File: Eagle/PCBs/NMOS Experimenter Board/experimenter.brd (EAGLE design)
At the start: 49.5 x 66 mm, 384 parts, among them Q10 2N7002, Q11 2N7002, Q12 2N7002, Q13 2N7002, Q14 2N7002, Q15 2N7002, Q16 2N7002, Q17 2N7002, Q18 2N7002, Q19 2N7002, Q2 2N7002, Q20 2N7002, Q21 2N7002, Q22 2N7002, Q23 2N7002, Q24 2N7002, Q25 2N7002, Q3 2N7002, Q4 2N7002, Q5 2N7002, Q6 2N7002, Q7 2N7002, Q8 2N7002, Q9 2N7002

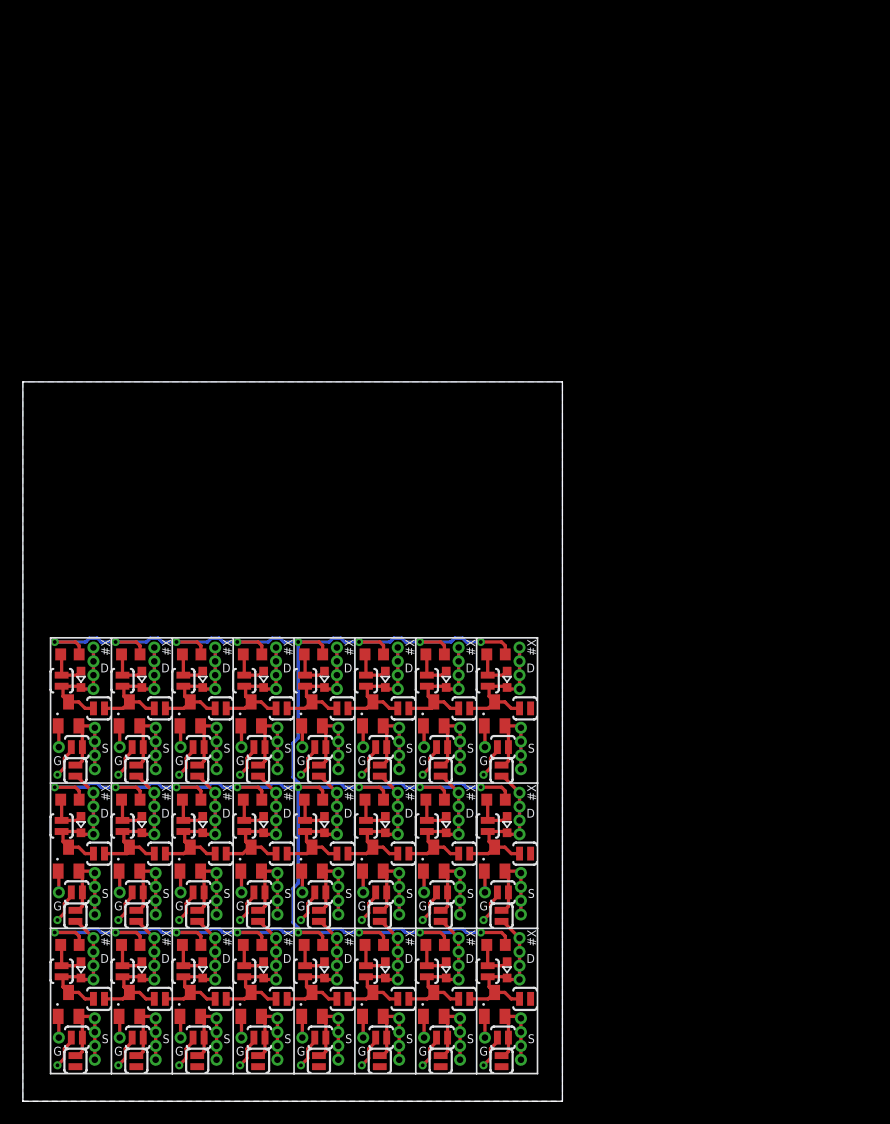
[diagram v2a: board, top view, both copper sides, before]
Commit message: A 6x12 grid fits
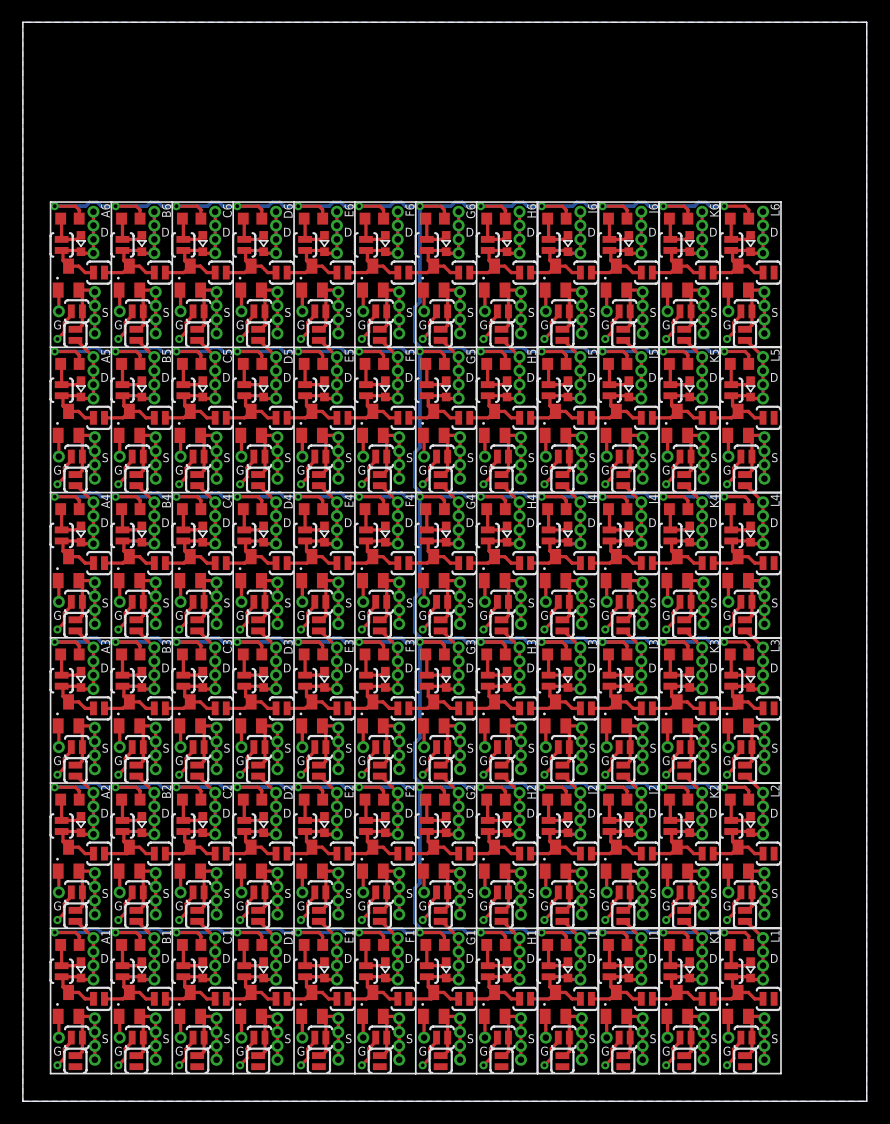
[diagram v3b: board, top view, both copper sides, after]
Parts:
- added D26, D27, D28, D29, D30, D31, D32, D33, D34, D35, D36, D37, D38, D39, D40, D41, D42, D43, D44, D45, D46, D47, D48, D49, D50, D51, D52, D53, D54, D55, D56, D57, D58, D59, D60, D61, D62, D63, D64, D65, D66, D67, D68, D69, D70, D71, D72, D73: (no value), ellajameson-core:CHIP-LED0603
- added DRAINA26, DRAINA27, DRAINA28, DRAINA29, DRAINA30, DRAINA31, DRAINA32, DRAINA33, DRAINA34, DRAINA35, DRAINA36, DRAINA37, DRAINA38, DRAINA39, DRAINA40, DRAINA41, DRAINA42, DRAINA43, DRAINA44, DRAINA45, DRAINA46, DRAINA47, DRAINA48, DRAINA49, DRAINA50, DRAINA51, DRAINA52, DRAINA53, DRAINA54, DRAINA55, DRAINA56, DRAINA57, DRAINA58, DRAINA59, DRAINA60, DRAINA61, DRAINA62, DRAINA63, DRAINA64, DRAINA65, DRAINA66, DRAINA67, DRAINA68, DRAINA69, DRAINA70, DRAINA71, DRAINA72, DRAINA73, DRAINB26, DRAINB27, DRAINB28, DRAINB29, DRAINB30, DRAINB31, DRAINB32, DRAINB33, DRAINB34, DRAINB35, DRAINB36, DRAINB37, DRAINB38, DRAINB39, DRAINB40, DRAINB41, DRAINB42, DRAINB43, DRAINB44, DRAINB45, DRAINB46, DRAINB47, DRAINB48, DRAINB49, DRAINB50, DRAINB51, DRAINB52, DRAINB53, DRAINB54, DRAINB55, DRAINB56, DRAINB57, DRAINB58, DRAINB59, DRAINB60, DRAINB61, DRAINB62, DRAINB63, DRAINB64, DRAINB65, DRAINB66, DRAINB67, DRAINB68, DRAINB69, DRAINB70, DRAINB71, DRAINB72, DRAINB73, DRAINC26, DRAINC27, DRAINC28, DRAINC29, DRAINC30, DRAINC31, DRAINC32, DRAINC33, DRAINC34, DRAINC35, DRAINC36, DRAINC37, DRAINC38, DRAINC39, DRAINC40, DRAINC41, DRAINC42, DRAINC43, DRAINC44, DRAINC45, DRAINC46, DRAINC47, DRAINC48, DRAINC49, DRAINC50, DRAINC51, DRAINC52, DRAINC53, DRAINC54, DRAINC55, DRAINC56, DRAINC57, DRAINC58, DRAINC59, DRAINC60, DRAINC61, DRAINC62, DRAINC63, DRAINC64, DRAINC65, DRAINC66, DRAINC67, DRAINC68, DRAINC69, DRAINC70, DRAINC71, DRAINC72, DRAINC73, DRAIND26, DRAIND27, DRAIND28, DRAIND29, DRAIND30, DRAIND31, DRAIND32, DRAIND33, DRAIND34, DRAIND35, DRAIND36, DRAIND37, DRAIND38, DRAIND39, DRAIND40, DRAIND41, DRAIND42, DRAIND43, DRAIND44, DRAIND45, DRAIND46, DRAIND47, DRAIND48, DRAIND49, DRAIND50, DRAIND51, DRAIND52, DRAIND53, DRAIND54, DRAIND55, DRAIND56, DRAIND57, DRAIND58, DRAIND59, DRAIND60, DRAIND61, DRAIND62, DRAIND63, DRAIND64, DRAIND65, DRAIND66, DRAIND67, DRAIND68, DRAIND69, DRAIND70, DRAIND71, DRAIND72, DRAIND73, GATE26, GATE27, GATE28, GATE29, GATE30, GATE31, GATE32, GATE33, GATE34, GATE35, GATE36, GATE37, GATE38, GATE39, GATE40, GATE41, GATE42, GATE43, GATE44, GATE45, GATE46, GATE47, GATE48, GATE49, GATE50, GATE51, GATE52, GATE53, GATE54, GATE55, GATE56, GATE57, GATE58, GATE59, GATE60, GATE61, GATE62, GATE63, GATE64, GATE65, GATE66, GATE67, GATE68, GATE69, GATE70, GATE71, GATE72, GATE73, SOURCEA26, SOURCEA27, SOURCEA28, SOURCEA29, SOURCEA30, SOURCEA31, SOURCEA32, SOURCEA33, SOURCEA34, SOURCEA35, SOURCEA36, SOURCEA37, SOURCEA38, SOURCEA39, SOURCEA40, SOURCEA41, SOURCEA42, SOURCEA43, SOURCEA44, SOURCEA45, SOURCEA46, SOURCEA47, SOURCEA48, SOURCEA49, SOURCEA50, SOURCEA51, SOURCEA52, SOURCEA53, SOURCEA54, SOURCEA55, SOURCEA56, SOURCEA57, SOURCEA58, SOURCEA59, SOURCEA60, SOURCEA61, SOURCEA62, SOURCEA63, SOURCEA64, SOURCEA65, SOURCEA66, SOURCEA67, SOURCEA68, SOURCEA69, SOURCEA70, SOURCEA71, SOURCEA72, SOURCEA73, SOURCEB26, SOURCEB27, SOURCEB28, SOURCEB29, SOURCEB30, SOURCEB31, SOURCEB32, SOURCEB33, SOURCEB34, SOURCEB35, SOURCEB36, SOURCEB37, SOURCEB38, SOURCEB39, SOURCEB40, SOURCEB41, SOURCEB42, SOURCEB43, SOURCEB44, SOURCEB45, SOURCEB46, SOURCEB47, SOURCEB48, SOURCEB49, SOURCEB50, SOURCEB51, SOURCEB52, SOURCEB53, SOURCEB54, SOURCEB55, SOURCEB56, SOURCEB57, SOURCEB58, SOURCEB59, SOURCEB60, SOURCEB61, SOURCEB62, SOURCEB63, SOURCEB64, SOURCEB65, SOURCEB66, SOURCEB67, SOURCEB68, SOURCEB69, SOURCEB70, SOURCEB71, SOURCEB72, SOURCEB73, SOURCEC26, SOURCEC27, SOURCEC28, SOURCEC29, SOURCEC30, SOURCEC31, SOURCEC32, SOURCEC33, SOURCEC34, SOURCEC35, SOURCEC36, SOURCEC37, SOURCEC38, SOURCEC39, SOURCEC40, SOURCEC41, SOURCEC42, SOURCEC43, SOURCEC44, SOURCEC45, SOURCEC46, SOURCEC47, SOURCEC48, SOURCEC49, SOURCEC50, SOURCEC51, SOURCEC52, SOURCEC53, SOURCEC54, SOURCEC55, SOURCEC56, SOURCEC57, SOURCEC58, SOURCEC59, SOURCEC60, SOURCEC61, SOURCEC62, SOURCEC63, SOURCEC64, SOURCEC65, SOURCEC66, SOURCEC67, SOURCEC68, SOURCEC69, SOURCEC70, SOURCEC71, SOURCEC72, SOURCEC73, SOURCED26, SOURCED27, SOURCED28, SOURCED29, SOURCED30, SOURCED31, SOURCED32, SOURCED33, SOURCED34, SOURCED35, SOURCED36, SOURCED37, SOURCED38, SOURCED39, SOURCED40, SOURCED41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: TPWIRE, ellajameson-core:TP_TH_WIRE
- added JD26, JD27, JD28, JD29, JD30, JD31, JD32, JD33, JD34, JD35, JD36, JD37, JD38, JD39, JD40, JD41, JD42, JD43, JD44, JD45, JD46, JD47, JD48, JD49, JD50, JD51, JD52, JD53, JD54, JD55, JD56, JD57, JD58, JD59, JD60, JD61, JD62, JD63, JD64, JD65, JD66, JD67, JD68, JD69, JD70, JD71, JD72, JD73, JN26, JN27, JN28, JN29, JN30, JN31, JN32, JN33, JN34, JN35, JN36, JN37, JN38, JN39, JN40, JN41, JN42, JN43, JN44, JN45, JN46, JN47, JN48, JN49, JN50, JN51, JN52, JN53, JN54, JN55, JN56, JN57, JN58, JN59, JN60, JN61, JN62, JN63, JN64, JN65, JN66, JN67, JN68, JN69, JN70, JN71, JN72, JN73, JP26, JP27, JP28, JP29, JP30, JP31, JP32, JP33, JP34, JP35, JP36, JP37, JP38, JP39, JP40, JP41, JP42, JP43, JP44, JP45, JP46, JP47, JP48, JP49, JP50, JP51, JP52, JP53, JP54, JP55, JP56, JP57, JP58, JP59, JP60, JP61, JP62, JP63, JP64, JP65, JP66, JP67, JP68, JP69, JP70, JP71, JP72, JP73, JS26, JS27, JS28, JS29, JS30, JS31, JS32, JS33, JS34, JS35, JS36, JS37, JS38, JS39, JS40, JS41, JS42, JS43, JS44, JS45, JS46, JS47, JS48, JS49, JS50, JS51, JS52, JS53, JS54, JS55, JS56, JS57, JS58, JS59, JS60, JS61, JS62, JS63, JS64, JS65, JS66, JS67, JS68, JS69, JS70, JS71, JS72, JS73: SJ_NO, ellajameson-core:SJ_2S-NO
- added Q26, Q27, Q28, Q29, Q30, Q31, Q32, Q33, Q34, Q35, Q36, Q37, Q38, Q39, Q40, Q41, Q42, Q43, Q44, Q45, Q46, Q47, Q48, Q49, Q50, Q51, Q52, Q53, Q54, Q55, Q56, Q57, Q58, Q59, Q60, Q61, Q62, Q63, Q64, Q65, Q66, Q67, Q68, Q69, Q70, Q71, Q72, Q73: 2N7002, ellajameson-core:SOT23
- added R26, R27, R28, R29, R30, R31, R32, R33, R34, R35, R36, R37, R38, R39, R40, R41, R42, R43, R44, R45, R46, R47, R48, R49, R50, R51, R52, R53, R54, R55, R56, R57, R58, R59, R60, R61, R62, R63, R64, R65, R66, R67, R68, R69, R70, R71, R72, R73: (no value), ellajameson-core:R0603
- moved DRAINA12 63.0 mm to (51.2, 81.7)
- moved DRAINA13 63.0 mm to (56.8, 81.7)
- moved DRAINB12 63.0 mm to (51.2, 80.4)
- moved DRAINB13 63.0 mm to (56.8, 80.4)
- moved DRAIND12 63.0 mm to (51.2, 77.9)
- moved DRAIND13 63.0 mm to (56.8, 77.9)
- moved JP12 63.0 mm to (48.3, 78.6)
- moved JP13 63.0 mm to (53.8, 78.6)
- moved JS12 63.0 mm to (49.5, 70.4)
- moved JS13 63.0 mm to (55.1, 70.4)
- moved SOURCEA12 63.0 mm to (51.3, 74.3)
- moved SOURCEA13 63.0 mm to (56.9, 74.3)
- moved SOURCEB12 63.0 mm to (51.3, 73.0)
- moved SOURCEB13 63.0 mm to (56.9, 73.0)
- moved SOURCED12 63.0 mm to (51.3, 70.5)
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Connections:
- new net N$101: D26.A, JP26.2, R26.1
- new net N$102: D26.C, DRAINA26.TP, DRAINB26.TP, DRAINC26.TP, DRAIND26.TP, JD26.2, JP26.1, JS34.1, Q26.3
- new net N$103: JN26.2, JS26.2, Q26.2, SOURCEA26.TP, SOURCEB26.TP, SOURCEC26.TP, SOURCED26.TP
- new net N$104: GATE26.TP, Q26.1
- new net N$105: D27.A, JP27.2, R27.1
- new net N$106: D27.C, DRAINA27.TP, DRAINB27.TP, DRAINC27.TP, DRAIND27.TP, JD26.1, JD27.2, JP27.1, JS35.1, Q27.3
- new net N$107: JN27.2, JS27.2, Q27.2, SOURCEA27.TP, SOURCEB27.TP, SOURCEC27.TP, SOURCED27.TP
- new net N$108: GATE27.TP, Q27.1
- new net N$109: D28.A, JP28.2, R28.1
- new net N$110: D28.C, DRAINA28.TP, DRAINB28.TP, DRAINC28.TP, DRAIND28.TP, JD27.1, JD28.2, JP28.1, JS36.1, Q28.3
- new net N$111: JN28.2, JS28.2, Q28.2, SOURCEA28.TP, SOURCEB28.TP, SOURCEC28.TP, SOURCED28.TP
- new net N$112: GATE28.TP, Q28.1
- new net N$113: D29.A, JP29.2, R29.1
- new net N$114: D29.C, DRAINA29.TP, DRAINB29.TP, DRAINC29.TP, DRAIND29.TP, JD28.1, JD29.2, JP29.1, JS37.1, Q29.3
- new net N$115: JN29.2, JS29.2, Q29.2, SOURCEA29.TP, SOURCEB29.TP, SOURCEC29.TP, SOURCED29.TP
- new net N$116: GATE29.TP, Q29.1
- new net N$117: D30.A, JP30.2, R30.1
- new net N$118: D30.C, DRAINA30.TP, DRAINB30.TP, DRAINC30.TP, DRAIND30.TP, JD29.1, JD30.2, JP30.1, JS38.1, Q30.3
- new net N$119: JN30.2, JS30.2, Q30.2, SOURCEA30.TP, SOURCEB30.TP, SOURCEC30.TP, SOURCED30.TP
- new net N$120: GATE30.TP, Q30.1
- new net N$121: D31.A, JP31.2, R31.1
- new net N$122: D31.C, DRAINA31.TP, DRAINB31.TP, DRAINC31.TP, DRAIND31.TP, JD30.1, JD31.2, JP31.1, JS39.1, Q31.3
- new net N$123: JN31.2, JS31.2, Q31.2, SOURCEA31.TP, SOURCEB31.TP, SOURCEC31.TP, SOURCED31.TP
- new net N$124: GATE31.TP, Q31.1
- new net N$125: D32.A, JP32.2, R32.1
- new net N$126: D32.C, DRAINA32.TP, DRAINB32.TP, DRAINC32.TP, DRAIND32.TP, JD31.1, JD32.2, JP32.1, JS40.1, Q32.3
- new net N$127: JN32.2, JS32.2, Q32.2, SOURCEA32.TP, SOURCEB32.TP, SOURCEC32.TP, SOURCED32.TP
- new net N$128: GATE32.TP, Q32.1
- new net N$129: D33.A, JP33.2, R33.1
- new net N$130: D33.C, DRAINA33.TP, DRAINB33.TP, DRAINC33.TP, DRAIND33.TP, JD32.1, JD33.2, JP33.1, JS41.1, Q33.3
- new net N$131: JN33.2, JS33.2, Q33.2, SOURCEA33.TP, SOURCEB33.TP, SOURCEC33.TP, SOURCED33.TP
- new net N$132: GATE33.TP, Q33.1
- new net N$133: D34.A, JP34.2, R34.1
- new net N$134: D34.C, DRAINA34.TP, DRAINB34.TP, DRAINC34.TP, DRAIND34.TP, JD34.2, JP34.1, JS42.1, Q34.3
- new net N$135: JN34.2, JS34.2, Q34.2, SOURCEA34.TP, SOURCEB34.TP, SOURCEC34.TP, SOURCED34.TP
- new net N$136: GATE34.TP, Q34.1
- new net N$137: D35.A, JP35.2, R35.1
- new net N$138: D35.C, DRAINA35.TP, DRAINB35.TP, DRAINC35.TP, DRAIND35.TP, JD34.1, JD35.2, JP35.1, JS43.1, Q35.3
- new net N$139: JN35.2, JS35.2, Q35.2, SOURCEA35.TP, SOURCEB35.TP, SOURCEC35.TP, SOURCED35.TP
- new net N$140: GATE35.TP, Q35.1
- new net N$141: D36.A, JP36.2, R36.1
- new net N$142: D36.C, DRAINA36.TP, DRAINB36.TP, DRAINC36.TP, DRAIND36.TP, JD35.1, JD36.2, JP36.1, JS44.1, Q36.3
- new net N$143: JN36.2, JS36.2, Q36.2, SOURCEA36.TP, SOURCEB36.TP, SOURCEC36.TP, SOURCED36.TP
- new net N$144: GATE36.TP, Q36.1
- new net N$145: D37.A, JP37.2, R37.1
- new net N$146: D37.C, DRAINA37.TP, DRAINB37.TP, DRAINC37.TP, DRAIND37.TP, JD36.1, JD37.2, JP37.1, JS45.1, Q37.3
- new net N$147: JN37.2, JS37.2, Q37.2, SOURCEA37.TP, SOURCEB37.TP, SOURCEC37.TP, SOURCED37.TP
- new net N$148: GATE37.TP, Q37.1
- new net N$149: D38.A, JP38.2, R38.1
- new net N$150: D38.C, DRAINA38.TP, DRAINB38.TP, DRAINC38.TP, DRAIND38.TP, JD37.1, JD38.2, JP38.1, JS46.1, Q38.3
- new net N$151: JN38.2, JS38.2, Q38.2, SOURCEA38.TP, SOURCEB38.TP, SOURCEC38.TP, SOURCED38.TP
- new net N$152: GATE38.TP, Q38.1
- new net N$153: D39.A, JP39.2, R39.1
- new net N$154: D39.C, DRAINA39.TP, DRAINB39.TP, DRAINC39.TP, DRAIND39.TP, JD38.1, JD39.2, JP39.1, JS47.1, Q39.3
- new net N$155: JN39.2, JS39.2, Q39.2, SOURCEA39.TP, SOURCEB39.TP, SOURCEC39.TP, SOURCED39.TP
- new net N$156: GATE39.TP, Q39.1
- new net N$157: D40.A, JP40.2, R40.1
- new net N$158: D40.C, DRAINA40.TP, DRAINB40.TP, DRAINC40.TP, DRAIND40.TP, JD39.1, JD40.2, JP40.1, JS48.1, Q40.3
- new net N$159: JN40.2, JS40.2, Q40.2, SOURCEA40.TP, SOURCEB40.TP, SOURCEC40.TP, SOURCED40.TP
- new net N$160: GATE40.TP, Q40.1
- new net N$161: D41.A, JP41.2, R41.1
- new net N$162: D41.C, DRAINA41.TP, DRAINB41.TP, DRAINC41.TP, DRAIND41.TP, JD40.1, JD41.2, JP41.1, JS49.1, Q41.3
- new net N$163: JN41.2, JS41.2, Q41.2, SOURCEA41.TP, SOURCEB41.TP, SOURCEC41.TP, SOURCED41.TP
- new net N$164: GATE41.TP, Q41.1
- new net N$165: D42.A, JP42.2, R42.1
- new net N$166: D42.C, DRAINA42.TP, DRAINB42.TP, DRAINC42.TP, DRAIND42.TP, JD42.2, JP42.1, JS50.1, Q42.3
- new net N$167: JN42.2, JS42.2, Q42.2, SOURCEA42.TP, SOURCEB42.TP, SOURCEC42.TP, SOURCED42.TP
- new net N$168: GATE42.TP, Q42.1
- new net N$169: D43.A, JP43.2, R43.1
- new net N$170: D43.C, DRAINA43.TP, DRAINB43.TP, DRAINC43.TP, DRAIND43.TP, JD42.1, JD43.2, JP43.1, JS51.1, Q43.3
- new net N$171: JN43.2, JS43.2, Q43.2, SOURCEA43.TP, SOURCEB43.TP, SOURCEC43.TP, SOURCED43.TP
- new net N$172: GATE43.TP, Q43.1
- new net N$173: D44.A, JP44.2, R44.1
- new net N$174: D44.C, DRAINA44.TP, DRAINB44.TP, DRAINC44.TP, DRAIND44.TP, JD43.1, JD44.2, JP44.1, JS52.1, Q44.3
- new net N$175: JN44.2, JS44.2, Q44.2, SOURCEA44.TP, SOURCEB44.TP, SOURCEC44.TP, SOURCED44.TP
- new net N$176: GATE44.TP, Q44.1
- new net N$177: D45.A, JP45.2, R45.1
- new net N$178: D45.C, DRAINA45.TP, DRAINB45.TP, DRAINC45.TP, DRAIND45.TP, JD44.1, JD45.2, JP45.1, JS53.1, Q45.3
- new net N$179: JN45.2, JS45.2, Q45.2, SOURCEA45.TP, SOURCEB45.TP, SOURCEC45.TP, SOURCED45.TP
- new net N$180: GATE45.TP, Q45.1
- new net N$181: D46.A, JP46.2, R46.1
- new net N$182: D46.C, DRAINA46.TP, DRAINB46.TP, DRAINC46.TP, DRAIND46.TP, JD45.1, JD46.2, JP46.1, JS54.1, Q46.3
- new net N$183: JN46.2, JS46.2, Q46.2, SOURCEA46.TP, SOURCEB46.TP, SOURCEC46.TP, SOURCED46.TP
- new net N$184: GATE46.TP, Q46.1
- new net N$185: D47.A, JP47.2, R47.1
- new net N$186: D47.C, DRAINA47.TP, DRAINB47.TP, DRAINC47.TP, DRAIND47.TP, JD46.1, JD47.2, JP47.1, JS55.1, Q47.3
- new net N$187: JN47.2, JS47.2, Q47.2, SOURCEA47.TP, SOURCEB47.TP, SOURCEC47.TP, SOURCED47.TP
- new net N$188: GATE47.TP, Q47.1
- new net N$189: D48.A, JP48.2, R48.1
- new net N$190: D48.C, DRAINA48.TP, DRAINB48.TP, DRAINC48.TP, DRAIND48.TP, JD47.1, JD48.2, JP48.1, JS56.1, Q48.3
- new net N$191: JN48.2, JS48.2, Q48.2, SOURCEA48.TP, SOURCEB48.TP, SOURCEC48.TP, SOURCED48.TP
- new net N$192: GATE48.TP, Q48.1
- new net N$193: D49.A, JP49.2, R49.1
- new net N$194: D49.C, DRAINA49.TP, DRAINB49.TP, DRAINC49.TP, DRAIND49.TP, JD48.1, JD49.2, JP49.1, JS57.1, Q49.3
- new net N$195: JN49.2, JS49.2, Q49.2, SOURCEA49.TP, SOURCEB49.TP, SOURCEC49.TP, SOURCED49.TP
- new net N$196: GATE49.TP, Q49.1
- new net N$197: D50.A, JP50.2, R50.1
- new net N$198: D50.C, DRAINA50.TP, DRAINB50.TP, DRAINC50.TP, DRAIND50.TP, JD50.2, JP50.1, JS58.1, Q50.3
- new net N$199: JN50.2, JS50.2, Q50.2, SOURCEA50.TP, SOURCEB50.TP, SOURCEC50.TP, SOURCED50.TP
- new net N$200: GATE50.TP, Q50.1
- new net N$201: D51.A, JP51.2, R51.1
- new net N$202: D51.C, DRAINA51.TP, DRAINB51.TP, DRAINC51.TP, DRAIND51.TP, JD50.1, JD51.2, JP51.1, JS59.1, Q51.3
- new net N$203: JN51.2, JS51.2, Q51.2, SOURCEA51.TP, SOURCEB51.TP, SOURCEC51.TP, SOURCED51.TP
- new net N$204: GATE51.TP, Q51.1
- new net N$205: D52.A, JP52.2, R52.1
- new net N$206: D52.C, DRAINA52.TP, DRAINB52.TP, DRAINC52.TP, DRAIND52.TP, JD51.1, JD52.2, JP52.1, JS60.1, Q52.3
- new net N$207: JN52.2, JS52.2, Q52.2, SOURCEA52.TP, SOURCEB52.TP, SOURCEC52.TP, SOURCED52.TP
- new net N$208: GATE52.TP, Q52.1
- new net N$209: D53.A, JP53.2, R53.1
- new net N$210: D53.C, DRAINA53.TP, DRAINB53.TP, DRAINC53.TP, DRAIND53.TP, JD52.1, JD53.2, JP53.1, JS61.1, Q53.3
- new net N$211: JN53.2, JS53.2, Q53.2, SOURCEA53.TP, SOURCEB53.TP, SOURCEC53.TP, SOURCED53.TP
- new net N$212: GATE53.TP, Q53.1
- new net N$213: D54.A, JP54.2, R54.1
- new net N$214: D54.C, DRAINA54.TP, DRAINB54.TP, DRAINC54.TP, DRAIND54.TP, JD53.1, JD54.2, JP54.1, JS62.1, Q54.3
- new net N$215: JN54.2, JS54.2, Q54.2, SOURCEA54.TP, SOURCEB54.TP, SOURCEC54.TP, SOURCED54.TP
- new net N$216: GATE54.TP, Q54.1
- new net N$217: D55.A, JP55.2, R55.1
- new net N$218: D55.C, DRAINA55.TP, DRAINB55.TP, DRAINC55.TP, DRAIND55.TP, JD54.1, JD55.2, JP55.1, JS63.1, Q55.3
- new net N$219: JN55.2, JS55.2, Q55.2, SOURCEA55.TP, SOURCEB55.TP, SOURCEC55.TP, SOURCED55.TP
- new net N$220: GATE55.TP, Q55.1
- new net N$221: D56.A, JP56.2, R56.1
- new net N$222: D56.C, DRAINA56.TP, DRAINB56.TP, DRAINC56.TP, DRAIND56.TP, JD55.1, JD56.2, JP56.1, JS64.1, Q56.3
- new net N$223: JN56.2, JS56.2, Q56.2, SOURCEA56.TP, SOURCEB56.TP, SOURCEC56.TP, SOURCED56.TP
- new net N$224: GATE56.TP, Q56.1
- new net N$225: D57.A, JP57.2, R57.1
- new net N$226: D57.C, DRAINA57.TP, DRAINB57.TP, DRAINC57.TP, DRAIND57.TP, JD56.1, JD57.2, JP57.1, JS65.1, Q57.3
- new net N$227: JN57.2, JS57.2, Q57.2, SOURCEA57.TP, SOURCEB57.TP, SOURCEC57.TP, SOURCED57.TP
- new net N$228: GATE57.TP, Q57.1
- new net N$229: D58.A, JP58.2, R58.1
- new net N$230: D58.C, DRAINA58.TP, DRAINB58.TP, DRAINC58.TP, DRAIND58.TP, JD58.2, JP58.1, Q58.3
- new net N$231: JN58.2, JS58.2, Q58.2, SOURCEA58.TP, SOURCEB58.TP, SOURCEC58.TP, SOURCED58.TP
- new net N$232: GATE58.TP, Q58.1
- new net N$233: D59.A, JP59.2, R59.1
- new net N$234: D59.C, DRAINA59.TP, DRAINB59.TP, DRAINC59.TP, DRAIND59.TP, JD58.1, JD59.2, JP59.1, Q59.3
- new net N$235: JN59.2, JS59.2, Q59.2, SOURCEA59.TP, SOURCEB59.TP, SOURCEC59.TP, SOURCED59.TP
- new net N$236: GATE59.TP, Q59.1
- new net N$237: D60.A, JP60.2, R60.1
- new net N$238: D60.C, DRAINA60.TP, DRAINB60.TP, DRAINC60.TP, DRAIND60.TP, JD59.1, JD60.2, JP60.1, Q60.3
- new net N$239: JN60.2, JS60.2, Q60.2, SOURCEA60.TP, SOURCEB60.TP, SOURCEC60.TP, SOURCED60.TP
- new net N$240: GATE60.TP, Q60.1
- new net N$241: D61.A, JP61.2, R61.1
- new net N$242: D61.C, DRAINA61.TP, DRAINB61.TP, DRAINC61.TP, DRAIND61.TP, JD60.1, JD61.2, JP61.1, Q61.3
- new net N$243: JN61.2, JS61.2, Q61.2, SOURCEA61.TP, SOURCEB61.TP, SOURCEC61.TP, SOURCED61.TP
- new net N$244: GATE61.TP, Q61.1
- new net N$245: D62.A, JP62.2, R62.1
- new net N$246: D62.C, DRAINA62.TP, DRAINB62.TP, DRAINC62.TP, DRAIND62.TP, JD61.1, JD62.2, JP62.1, Q62.3
- new net N$247: JN62.2, JS62.2, Q62.2, SOURCEA62.TP, SOURCEB62.TP, SOURCEC62.TP, SOURCED62.TP
- new net N$248: GATE62.TP, Q62.1
- new net N$249: D63.A, JP63.2, R63.1
- new net N$250: D63.C, DRAINA63.TP, DRAINB63.TP, DRAINC63.TP, DRAIND63.TP, JD62.1, JD63.2, JP63.1, Q63.3
- new net N$251: JN63.2, JS63.2, Q63.2, SOURCEA63.TP, SOURCEB63.TP, SOURCEC63.TP, SOURCED63.TP
- new net N$252: GATE63.TP, Q63.1
- new net N$253: D64.A, JP64.2, R64.1
- new net N$254: D64.C, DRAINA64.TP, DRAINB64.TP, DRAINC64.TP, DRAIND64.TP, JD63.1, JD64.2, JP64.1, Q64.3
- new net N$255: JN64.2, JS64.2, Q64.2, SOURCEA64.TP, SOURCEB64.TP, SOURCEC64.TP, SOURCED64.TP
- new net N$256: GATE64.TP, Q64.1
- new net N$257: D65.A, JP65.2, R65.1
- new net N$258: D65.C, DRAINA65.TP, DRAINB65.TP, DRAINC65.TP, DRAIND65.TP, JD64.1, JD65.2, JP65.1, Q65.3
- new net N$259: JN65.2, JS65.2, Q65.2, SOURCEA65.TP, SOURCEB65.TP, SOURCEC65.TP, SOURCED65.TP
- new net N$260: GATE65.TP, Q65.1
- new net N$261: D66.A, JP66.2, R66.1
- new net N$262: D66.C, DRAINA66.TP, DRAINB66.TP, DRAINC66.TP, DRAIND66.TP, JD66.2, JD7.1, JP66.1, JS68.1, Q66.3
- new net N$263: JN66.2, JS66.2, Q66.2, SOURCEA66.TP, SOURCEB66.TP, SOURCEC66.TP, SOURCED66.TP
- new net N$264: GATE66.TP, Q66.1
- new net N$265: D67.A, JP67.2, R67.1
- new net N$266: D67.C, DRAINA67.TP, DRAINB67.TP, DRAINC67.TP, DRAIND67.TP, JD66.1, JD67.2, JP67.1, JS69.1, Q67.3
- new net N$267: JN67.2, JS67.2, Q67.2, SOURCEA67.TP, SOURCEB67.TP, SOURCEC67.TP, SOURCED67.TP
- new net N$268: GATE67.TP, Q67.1
- new net N$269: D68.A, JP68.2, R68.1
- new net N$270: D68.C, DRAINA68.TP, DRAINB68.TP, DRAINC68.TP, DRAIND68.TP, JD68.2, JD9.1, JP68.1, JS70.1, Q68.3
- new net N$271: JN68.2, JS68.2, Q68.2, SOURCEA68.TP, SOURCEB68.TP, SOURCEC68.TP, SOURCED68.TP
- new net N$272: GATE68.TP, Q68.1
- new net N$273: D69.A, JP69.2, R69.1
- new net N$274: D69.C, DRAINA69.TP, DRAINB69.TP, DRAINC69.TP, DRAIND69.TP, JD68.1, JD69.2, JP69.1, JS71.1, Q69.3
- new net N$275: JN69.2, JS69.2, Q69.2, SOURCEA69.TP, SOURCEB69.TP, SOURCEC69.TP, SOURCED69.TP
- new net N$276: GATE69.TP, Q69.1
- new net N$277: D70.A, JP70.2, R70.1
- new net N$278: D70.C, DRAINA70.TP, DRAINB70.TP, DRAINC70.TP, DRAIND70.TP, JD11.1, JD70.2, JP70.1, JS72.1, Q70.3
- new net N$279: JN70.2, JS70.2, Q70.2, SOURCEA70.TP, SOURCEB70.TP, SOURCEC70.TP, SOURCED70.TP
- new net N$280: GATE70.TP, Q70.1
- new net N$281: D71.A, JP71.2, R71.1
- new net N$282: D71.C, DRAINA71.TP, DRAINB71.TP, DRAINC71.TP, DRAIND71.TP, JD70.1, JD71.2, JP71.1, JS73.1, Q71.3
- new net N$283: JN71.2, JS71.2, Q71.2, SOURCEA71.TP, SOURCEB71.TP, SOURCEC71.TP, SOURCED71.TP
- new net N$284: GATE71.TP, Q71.1
- new net N$285: D72.A, JP72.2, R72.1
- new net N$286: D72.C, DRAINA72.TP, DRAINB72.TP, DRAINC72.TP, DRAIND72.TP, JD13.1, JD72.2, JP72.1, Q72.3
- new net N$287: JN72.2, JS72.2, Q72.2, SOURCEA72.TP, SOURCEB72.TP, SOURCEC72.TP, SOURCED72.TP
- new net N$288: GATE72.TP, Q72.1
- new net N$289: D73.A, JP73.2, R73.1
- new net N$290: D73.C, DRAINA73.TP, DRAINB73.TP, DRAINC73.TP, DRAIND73.TP, JD72.1, JD73.2, JP73.1, Q73.3
- new net N$291: JN73.2, JS73.2, Q73.2, SOURCEA73.TP, SOURCEB73.TP, SOURCEC73.TP, SOURCED73.TP
- new net N$292: GATE73.TP, Q73.1
- net GND: now also JN26.1, JN27.1, JN28.1, JN29.1, JN30.1, JN31.1, JN32.1, JN33.1, JN34.1, JN35.1, JN36.1, JN37.1, JN38.1, JN39.1, JN40.1, JN41.1, JN42.1, JN43.1, JN44.1, JN45.1, JN46.1, JN47.1, JN48.1, JN49.1, JN50.1, JN51.1, JN52.1, JN53.1, JN54.1, JN55.1, JN56.1, JN57.1, JN58.1, JN59.1, JN60.1, JN61.1, JN62.1, JN63.1, JN64.1, JN65.1, JN66.1, JN67.1, JN68.1, JN69.1, JN70.1, JN71.1, JN72.1, JN73.1
- net N$10: now also JD2.1, JS5.1; no longer JD4.1, JS12.1
- net N$14: now also JD33.1, JS6.1; no longer JD2.1, JS11.1
- net N$18: now also JD4.1, JS7.1; no longer JD3.1, JS13.1
- net N$2: now also JD25.1, JS4.1; no longer JS10.1
- net N$22: now also JD41.1, JS8.1; no longer JD5.1, JS14.1
- net N$26: now also JS9.1; no longer JS15.1
- net N$30: now also JD49.1, JS10.1; no longer JD7.1, JS16.1
- net N$34: now also JS11.1; no longer JS17.1
- net N$38: now also JD57.1, JS12.1; no longer JS18.1
- net N$42: now also JS13.1; no longer JS19.1
- net N$46: now also JD65.1; no longer JD11.1, JS20.1
- net N$50: no longer JS21.1
- net N$54: now also JD3.1, JS17.1; no longer JD13.1, JS22.1
- net N$58: now also JS16.1; no longer JS23.1
- net N$62: now also JD17.1, JS67.1; no longer JD15.1, JS24.1
- net N$66: now also JD5.1, JS66.1; no longer JD16.1, JS25.1
- net N$70: now also JS26.1
- net N$74: now also JS27.1
- net N$78: now also JS28.1
- net N$82: now also JS29.1
- net N$86: now also JS30.1
- net N$90: now also JS31.1
- net N$94: now also JS32.1
- net N$98: now also JS33.1
- net VCC: now also R26.2, R27.2, R28.2, R29.2, R30.2, R31.2, R32.2, R33.2, R34.2, R35.2, R36.2, R37.2, R38.2, R39.2, R40.2, R41.2, R42.2, R43.2, R44.2, R45.2, R46.2, R47.2, R48.2, R49.2, R50.2, R51.2, R52.2, R53.2, R54.2, R55.2, R56.2, R57.2, R58.2, R59.2, R60.2, R61.2, R62.2, R63.2, R64.2, R65.2, R66.2, R67.2, R68.2, R69.2, R70.2, R71.2, R72.2, R73.2
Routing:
- net VCC: track 227.5 -> 686.3 mm, vias 24 -> 72
- net GND: track 73.6 -> 220.8 mm, vias 24 -> 72
- net N$266: track 0.00 -> 16.2 mm
- net N$106: track 0.00 -> 16.2 mm
- net N$182: track 0.00 -> 16.0 mm
- net N$118: track 0.00 -> 16.0 mm
- net N$194: track 0.00 -> 15.8 mm
- net N$162: track 0.00 -> 15.8 mm
- net N$190: track 0.00 -> 15.8 mm
- net N$186: track 0.00 -> 15.8 mm
- net N$158: track 0.00 -> 15.8 mm
- net N$154: track 0.00 -> 15.8 mm
- net N$130: track 0.00 -> 15.8 mm
- net N$122: track 0.00 -> 15.8 mm
- net N$174: track 0.00 -> 15.8 mm
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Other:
- board size 49.5 x 66 mm -> 77.5 x 99.1 mm
- board text added: "A1"
- board text added: "A2"
- board text added: "A3"
- board text added: "A4"
- board text added: "A5"
- board text added: "A6"
- board text added: "B1"
- board text added: "B2"
- board text added: "B3"
- board text added: "B4"
- board text added: "B5"
- board text added: "B6"
- board text added: "C1"
- board text added: "C2"
- board text added: "C3"
- board text added: "C4"
- board text added: "C5"
- board text added: "C6"
- board text added: "D1"
- board text added: "D2"
- board text added: "D3"
- board text added: "D4"
- board text added: "D5"
- board text added: "D6"
- board text added: "E1"
- board text added: "E2"
- board text added: "E3"
- board text added: "E4"
- board text added: "E5"
- board text added: "E6"
- board text added: "F1"
- board text added: "F2"
- board text added: "F3"
- board text added: "F4"
- board text added: "F5"
- board text added: "F6"
- board text added: "G1"
- board text added: "G2"
- board text added: "G3"
- board text added: "G4"
- board text added: "G5"
- board text added: "G6"
- board text added: "H1"
- board text added: "H2"
- board text added: "H3"
- board text added: "H4"
- board text added: "H5"
- board text added: "H6"
- board text added: "I1"
- board text added: "I2"
- board text added: "I3"
- board text added: "I4"
- board text added: "I5"
- board text added: "I6"
- board text added: "J1"
- board text added: "J2"
- board text added: "J3"
- board text added: "J4"
- board text added: "J5"
- board text added: "J6"
- board text added: "K1"
- board text added: "K2"
- board text added: "K3"
- board text added: "K4"
- board text added: "K5"
- board text added: "K6"
- board text added: "L1"
- board text added: "L2"
- board text added: "L3"
- board text added: "L4"
- board text added: "L5"
- board text added: "L6"
- board text removed: "#X"

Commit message: Removed useless jumpers
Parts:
- removed JD15, JD16, JD67, JD69, JD71, JD73, JS14, JS15, JS18, JS19, JS2, JS20, JS21, JS22, JS23, JS24, JS25, JS3: SJ_NO, ellajameson-core:SJ_2S-NO
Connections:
- net N$11: no longer JS3.2
- net N$266: no longer JD67.2
- net N$274: no longer JD69.2
- net N$282: no longer JD71.2
- net N$290: no longer JD73.2
- net N$3: no longer JS2.2
- net N$55: no longer JS14.2
- net N$58: no longer JD15.2
- net N$59: no longer JS15.2
- net N$62: no longer JD16.2
- net N$71: no longer JS18.2
- net N$75: no longer JS19.2
- net N$79: no longer JS20.2
- net N$83: no longer JS21.2
- net N$87: no longer JS22.2
- net N$91: no longer JS23.2
- net N$95: no longer JS24.2
- net N$99: no longer JS25.2
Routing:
- net N$266: track 16.2 -> 13.3 mm
- net N$290: track 13.5 -> 11.0 mm
- net N$58: track 15.8 -> 13.3 mm
- net N$62: track 15.8 -> 13.3 mm
- net N$282: track 15.8 -> 13.3 mm
- net N$274: track 15.8 -> 13.3 mm
- net N$91: track 9.49 -> 7.42 mm
- net N$59: track 9.49 -> 7.42 mm
- net N$79: track 9.49 -> 7.42 mm
- net N$83: track 9.49 -> 7.42 mm
- net N$99: track 9.49 -> 7.42 mm
- net N$71: track 9.49 -> 7.42 mm
- net N$55: track 9.49 -> 7.42 mm
- net N$3: track 9.49 -> 7.42 mm
- net N$11: track 9.49 -> 7.42 mm
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
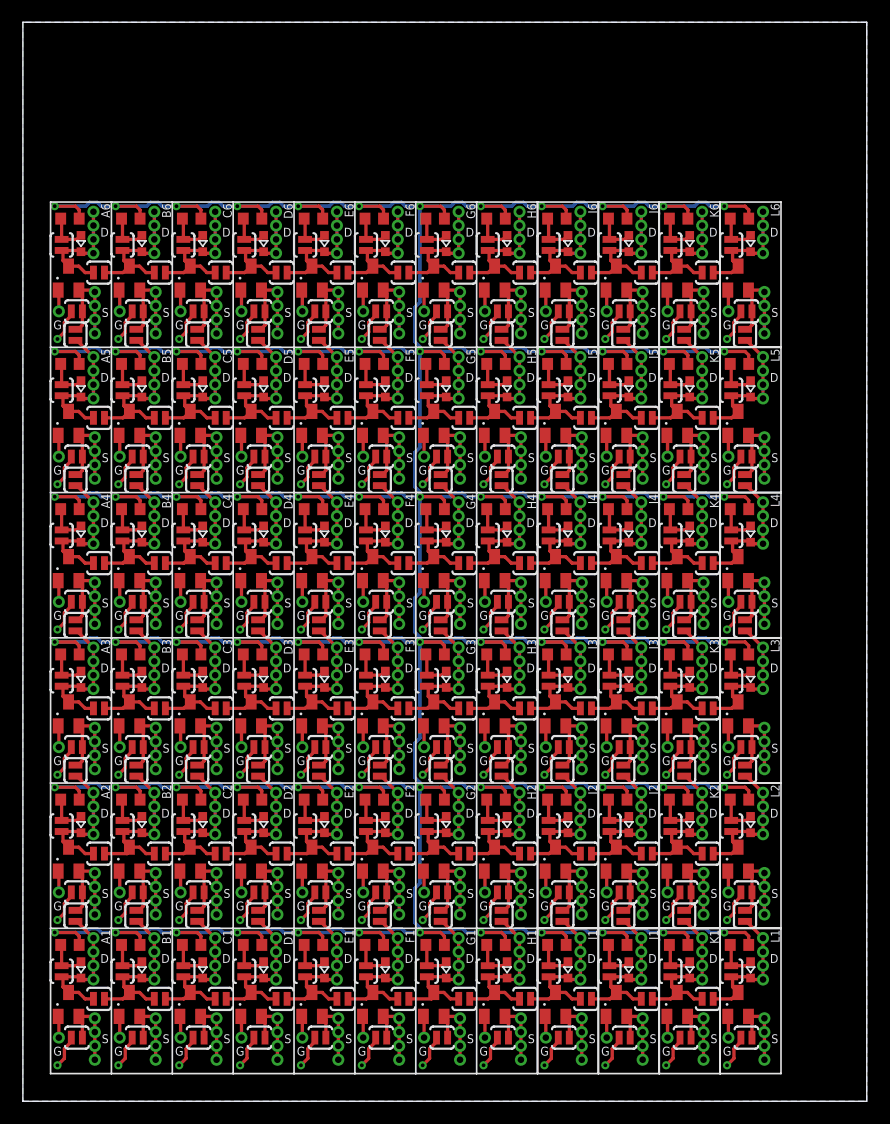
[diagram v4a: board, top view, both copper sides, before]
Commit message: Added 6x buttons with debouncing
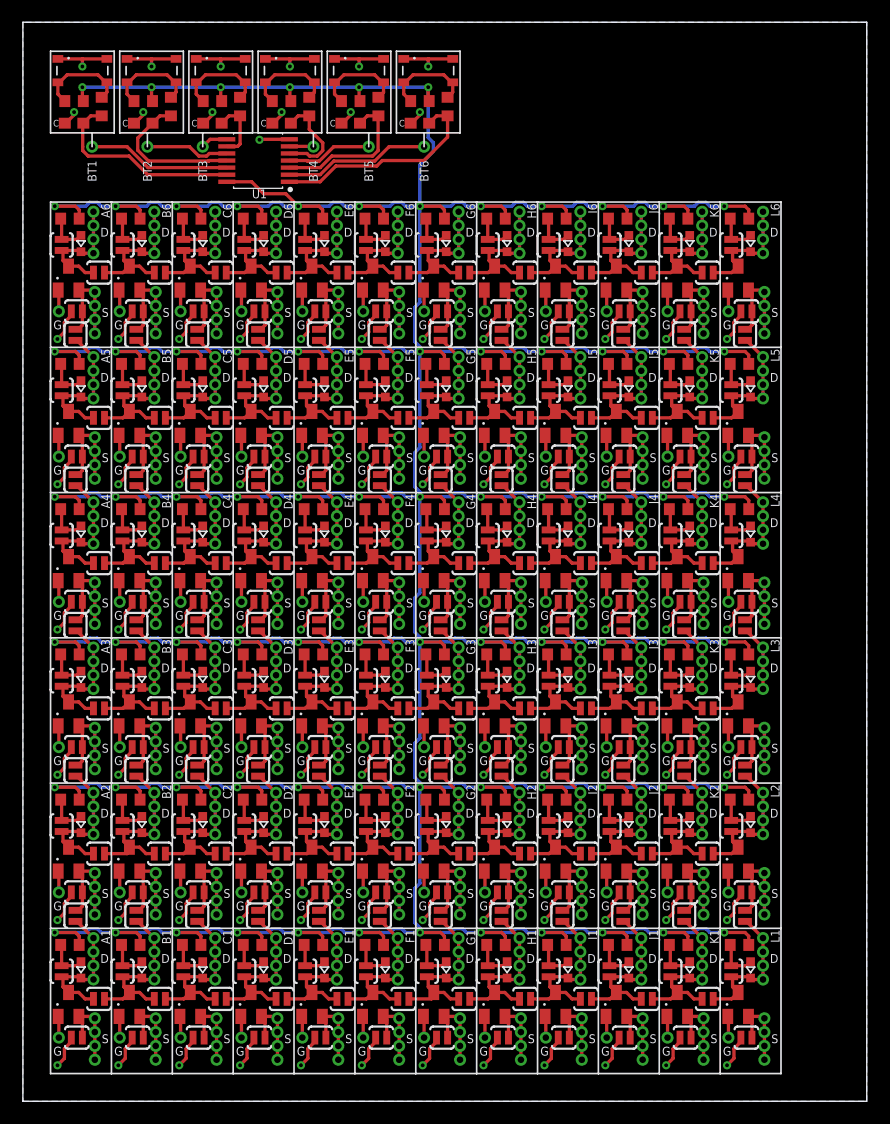
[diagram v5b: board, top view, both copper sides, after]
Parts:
- added B1, B2, B3, B4, B5, B6: TPWIRE, ellajameson-core:TP_TH_WIRE
- added C11, C2, C3, C5, C7, C9: 0.1u, ellajameson-core:C0603
- added R75, R76, R77, R78, R81, R82, R85, R86, R89, R90, R93, R94: 10k, ellajameson-core:R0603
- added S11, S2, S3, S5, S7, S9: (no value), ellajameson-core:SW4_PTS815_SJM_250_SMTR_LFS_CN
- added U1: 74HC14PW, ellajameson-core:TSSOP14
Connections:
- new net N$293: R77.1, R78.2, S3.3, S3.4
- new net N$294: C3.1, R78.1, U1.11
- new net N$295: B4.TP, U1.6
- new net N$296: B3.TP, U1.8
- new net N$297: R81.1, R82.2, S5.3, S5.4
- new net N$298: C5.1, R82.1, U1.9
- new net N$299: B2.TP, U1.10
- new net N$300: B1.TP, U1.12
- new net N$301: R85.1, R86.2, S7.3, S7.4
- new net N$302: C7.1, R86.1, U1.5
- new net N$305: R89.1, R90.2, S9.3, S9.4
- new net N$306: C9.1, R90.1, U1.3
- new net N$309: R93.1, R94.2, S11.3, S11.4
- new net N$310: C11.1, R94.1, U1.1
- new net N$5: B6.TP, U1.2
- new net N$6: B5.TP, U1.4
- new net N$7: R75.1, R76.2, S2.3, S2.4
- new net N$8: C2.1, R76.1, U1.13
- net GND: now also C11.2, C2.2, C3.2, C5.2, C7.2, C9.2, S11.1, S11.2, S2.1, S2.2, S3.1, S3.2, S5.1, S5.2, S7.1, S7.2, S9.1, S9.2, U1.7
- net VCC: now also R75.2, R77.2, R81.2, R85.2, R89.2, R93.2, U1.14
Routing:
- net VCC: track 686.3 -> 745.0 mm, vias 72 -> 78
- net GND: track 220.8 -> 263.2 mm, vias 72 -> 85
- net N$310: track 0.00 -> 20.1 mm
- net N$8: track 0.00 -> 18.7 mm
- net N$306: track 0.00 -> 14.0 mm
- net N$294: track 0.00 -> 13.6 mm
- net N$5: track 0.00 -> 13.4 mm
- net N$300: track 0.00 -> 13.2 mm
- net N$302: track 0.00 -> 9.05 mm
- net N$297: track 0.00 -> 8.63 mm
- net N$7: track 0.00 -> 8.63 mm
- net N$301: track 0.00 -> 8.63 mm
- net N$293: track 0.00 -> 8.63 mm
- net N$309: track 0.00 -> 8.63 mm
- net N$305: track 0.00 -> 8.63 mm
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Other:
- board text added: "BT1"
- board text added: "BT2"
- board text added: "BT3"
- board text added: "BT4"
- board text added: "BT5"
- board text added: "BT6"
- board text added: "C"

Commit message: Added basic power and stripboard
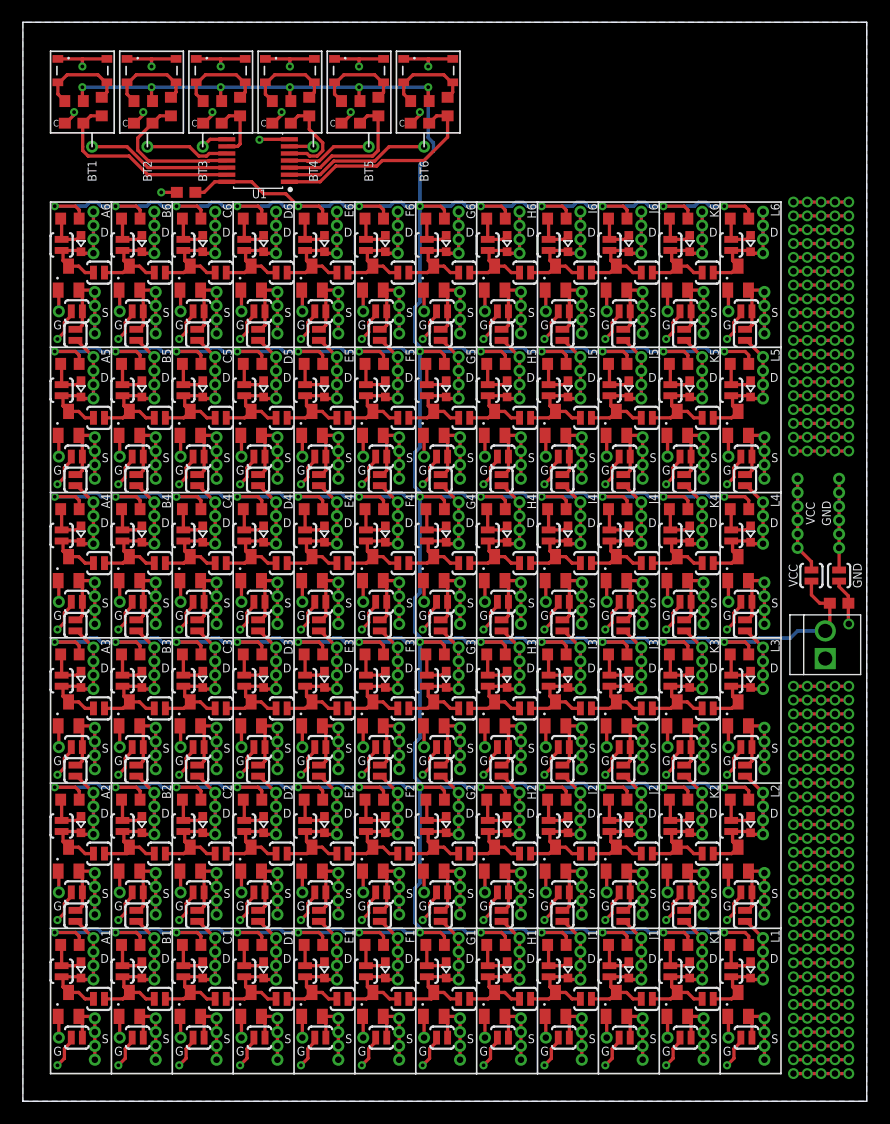
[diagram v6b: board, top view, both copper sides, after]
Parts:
- added C1, C4: 0.1u, ellajameson-core:C0603
- added J1: (no value), ellajameson-core:OSTVN02A150
- added SJ1, SJ2: SJ_NO, ellajameson-core:SJ_2S-NO
- added VCC1, VCC2, VCC3, VCC4, VCC5, VCC6, VSS1, VSS2, VSS3, VSS4, VSS5, VSS6: TPWIRE, ellajameson-core:TP_TH_WIRE
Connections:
- new net N$303: SJ2.2, VCC1.TP, VCC2.TP, VCC3.TP, VCC4.TP, VCC5.TP, VCC6.TP
- new net N$304: SJ1.1, VSS1.TP, VSS2.TP, VSS3.TP, VSS4.TP, VSS5.TP, VSS6.TP
- net GND: now also C1.2, C4.1, J1.P$1, SJ1.2
- net VCC: now also C1.1, C4.2, J1.P$2, SJ2.1
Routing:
- net VCC: track 745.0 -> 764.0 mm
- net N$303: track 0.00 -> 8.91 mm
- net N$304: track 0.00 -> 8.38 mm
- net GND: track 263.2 -> 268.9 mm, vias 85 -> 87
- net BB9: track 0.00 -> 5.08 mm, vias 0 -> 5
- net BB8: track 0.00 -> 5.08 mm, vias 0 -> 5
- net BB7: track 0.00 -> 5.08 mm, vias 0 -> 5
- net BB6: track 0.00 -> 5.08 mm, vias 0 -> 5
- net BB5: track 0.00 -> 5.08 mm, vias 0 -> 5
- net BB48: track 0.00 -> 5.08 mm, vias 0 -> 5
- net BB47: track 0.00 -> 5.08 mm, vias 0 -> 5
- net BB46: track 0.00 -> 5.08 mm, vias 0 -> 5
- net BB45: track 0.00 -> 5.08 mm, vias 0 -> 5
- net BB44: track 0.00 -> 5.08 mm, vias 0 -> 5
- net BB43: track 0.00 -> 5.08 mm, vias 0 -> 5
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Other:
- board text added: "GND"
- board text added: "VCC"
